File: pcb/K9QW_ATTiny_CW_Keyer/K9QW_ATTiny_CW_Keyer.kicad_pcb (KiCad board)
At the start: 2 copper layers, 50.8 x 31.8 mm, 33 parts, among them J1 Power Input, J2 AudioJack4, J3 AudioJack4, J4 Sidetone, J5 Mounting Hole, Q1 AO3401A, Q2 MMBT3904, Q3 MMBT2222A, Q4 MMBT3904, SW1 Power Switch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

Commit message: Routing signals
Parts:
- moved R4 25.6 mm to (151.8, 90.4), turned to 0 degrees
- moved Q2 24.4 mm to (155.8, 91.3)
- moved C6 16.0 mm to (161.4, 107.1), turned to 180 degrees
- moved Q3 9.10 mm to (146.3, 91.4), turned to -90 degrees
- moved D2 1.00 mm to (173.6, 97.6), turned to 180 degrees
- moved R5 0.66 mm to (169.3, 97.6)
- moved R3 0.10 mm to (155.3, 105.4)
- moved Q1 0.06 mm to (136.6, 106.1)
- turned R6 to 180 degrees
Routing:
- net Net-(Q3-C): track 0.21 -> 56.2 mm
- net VCC: track 0.15 -> 52.1 mm
- net COMMAND: track 0.00 -> 29.3 mm
- net Net-(D2-K): track 0.00 -> 25.6 mm
- net Net-(D1-K): track 0.00 -> 22.8 mm
- net SIDETONE: track 0.00 -> 21.2 mm
- net VDC: track 0.00 -> 15.4 mm
- net Net-(D3-K): track 0.00 -> 14.9 mm
- net Net-(JP1-A): track 0.00 -> 14.7 mm
- net DAH: track 0.00 -> 14.5 mm
- net DIT: track 0.00 -> 9.48 mm
- net KEY: track 0.00 -> 5.96 mm
- net Net-(D1-A): track 0.00 -> 5.27 mm
- net Net-(SW1-A): track 0.00 -> 5.18 mm
- net Net-(Q3-B): track 0.02 -> 4.41 mm
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
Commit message: Refining layout
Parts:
- moved Q4 10.9 mm to (151.0, 113.7), turned to -90 degrees
- moved SW2 7.91 mm to (167.7, 111.2), turned to 0 degrees
- moved R8 6.43 mm to (155.3, 107.1), turned to 180 degrees
- moved R7 5.73 mm to (153.9, 113.6), turned to 90 degrees
- moved D3 4.91 mm to (153.9, 109.9)
- moved J4 4.45 mm to (158.5, 111.3), turned to 0 degrees
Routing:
- net Net-(D3-K): track 14.9 -> 5.82 mm
- net SIDETONE: track 21.2 -> 25.0 mm
- net COMMAND: track 29.3 -> 27.4 mm
- net VCC: track 52.1 -> 53.9 mm
- net Net-(D3-A): track 1.90 -> 3.12 mm
- net GND: track 0.00 -> 0.83 mm, vias 8 -> 6
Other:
- board text added: "S"

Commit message: Minor adjustments
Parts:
- moved C1 4.72 mm to (148.4, 102.7), turned to 180 degrees
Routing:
- net VCC: track 53.9 -> 54.5 mm
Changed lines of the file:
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@@
 	(footprint "Capacitor_SMD:C_0603_1608Metric_Pad1.08x0.95mm_HandSolder"
 		(layer "F.Cu")
-		(at 151.5364 106.2239 -90)
+		(at 148.4122 102.6922 180)
 		(descr "Capacitor SMD 0603 (1608 Metric), square (rectangular) end terminal, IPC_7351 nominal with elongated pad for handsoldering. (Body size source: IPC-SM-782 page 76, https://www.pcb-3d.com/wordpress/wp-content/uploads/ipc-sm-782a_amendment_1_and_2.pdf), generated with kicad-footprint-generator")
 		(tags "capacitor handsolder")
 		(property "Reference" "C1"
-			(at -0.0011 -1.4732 90)
+			(at -0.0011 -1.4732 360)
 			(layer "F.SilkS")
 			(effects
@@
 		)
 		(property "Value" "100nF"
-			(at 0 1.43 90)
+			(at 0 1.43 360)
 			(layer "F.Fab")
 			(effects
@@
 		)
 		(property "Footprint" "Capacitor_SMD:C_0603_1608Metric_Pad1.08x0.95mm_HandSolder"
-			(at 0 0 -90)
+			(at 0 0 180)
 			(unlocked yes)
 			(layer "F.Fab")
@@
 		)
 		(property "Datasheet" ""
-			(at 0 0 -90)
+			(at 0 0 180)
 			(unlocked yes)
 			(layer "F.Fab")
@@
 		)
 		(property "Description" "Unpolarized capacitor"
-			(at 0 0 -90)
+			(at 0 0 180)
 			(unlocked yes)
 			(layer "F.Fab")
@@
 		)
 		(fp_line
-			(start -1.65 0.73)
-			(end -1.65 -0.73)
+			(start 1.65 0.73)
+			(end -1.65 0.73)
 			(stroke
 				(width 0.05)
@@
 		)
 		(fp_line
-			(start 1.65 0.73)
-			(end -1.65 0.73)
+			(start 1.65 -0.73)
+			(end 1.65 0.73)
 			(stroke
 				(width 0.05)
@@
 		)
 		(fp_line
-			(start -1.65 -0.73)
-			(end 1.65 -0.73)
+			(start -1.65 0.73)
+			(end -1.65 -0.73)
 			(stroke
 				(width 0.05)
@@
 		)
 		(fp_line
-			(start 1.65 -0.73)
-			(end 1.65 0.73)
+			(start -1.65 -0.73)
+			(end 1.65 -0.73)
 			(stroke
 				(width 0.05)
@@
 		)
 		(fp_line
-			(start -0.8 0.4)
-			(end -0.8 -0.4)
+			(start 0.8 0.4)
+			(end -0.8 0.4)
 			(stroke
 				(width 0.1)
@@
 		)
 		(fp_line
-			(start 0.8 0.4)
-			(end -0.8 0.4)
+			(start 0.8 -0.4)
+			(end 0.8 0.4)
 			(stroke
 				(width 0.1)
@@
 		)
 		(fp_line
-			(start -0.8 -0.4)
-			(end 0.8 -0.4)
+			(start -0.8 0.4)
+			(end -0.8 -0.4)
 			(stroke
 				(width 0.1)
@@
 		)
 		(fp_line
-			(start 0.8 -0.4)
-			(end 0.8 0.4)
+			(start -0.8 -0.4)
+			(end 0.8 -0.4)
 			(stroke
 				(width 0.1)
@@
 		)
 		(fp_text user "${REFERENCE}"
-			(at 0 0 90)
+			(at 0 0 360)
 			(layer "F.Fab")
 			(effects
@@
 		)
 		(pad "1" smd roundrect
-			(at -0.8625 0 270)
+			(at -0.8625 0 180)
 			(size 1.075 0.95)
 			(layers "F.Cu" "F.Paste" "F.Mask")
@@
 		)
 		(pad "2" smd roundrect
-			(at 0.8625 0 270)
+			(at 0.8625 0 180)
 			(size 1.075 0.95)
 			(layers "F.Cu" "F.Paste" "F.Mask")
@@
 	)
 	(segment
+		(start 151.7612 102.6884)
+		(end 151.401 102.6884)
+		(width 0.2)
+		(layer "F.Cu")
+		(net 1)
+	)
+	(segment
+		(start 149.2785 102.6884)
+		(end 149.2747 102.6922)
+		(width 1)
+		(layer "F.Cu")
+		(net 1)
+	)
+	(segment
+		(start 154.4358 105.3592)
+		(end 154.432 105.3592)
+		(width 0.2)
+		(layer "F.Cu")
+		(net 1)
+	)
+	(segment
 		(start 139.461 110.744)
 		(end 137.175 113.03)
@@
 	)
 	(segment
-		(start 151.5364 102.8238)
-		(end 151.401 102.6884)
-		(width 1)
+		(start 154.432 105.3592)
+		(end 151.7612 102.6884)
+		(width 0.2)
 		(layer "F.Cu")
 		(net 1)
 	)
 	(segment
-		(start 151.5364 105.3614)
-		(end 154.4336 105.3614)
-		(width 0.2)
+		(start 151.5364 102.8238)
+		(end 151.401 102.6884)
+		(width 1)
 		(layer "F.Cu")
 		(net 1)
@@
 	)
 	(segment
-		(start 151.6434 105.2544)
-		(end 151.5364 105.3614)
-		(width 0.2)
-		(layer "F.Cu")
-		(net 1)
-	)
-	(segment
 		(start 164.7314 106.1342)
 		(end 168.4058 102.4598)
@@
 	)
 	(segment
-		(start 151.5364 105.3614)
-		(end 151.5364 102.8238)
+		(start 146.5315 110.7455)
+		(end 146.533 110.744)
 		(width 1)
 		(layer "F.Cu")
@@
 	)
 	(segment
-		(start 146.5315 110.7455)
-		(end 146.533 110.744)
+		(start 151.401 102.6884)
+		(end 149.2785 102.6884)
 		(width 1)
 		(layer "F.Cu")

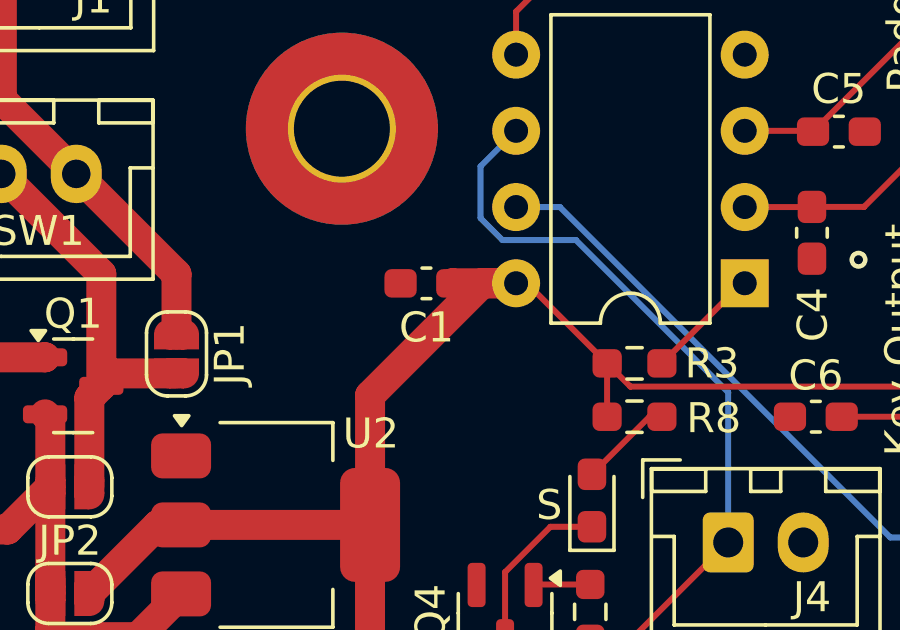
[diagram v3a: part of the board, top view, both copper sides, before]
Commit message: Filter cap for command button
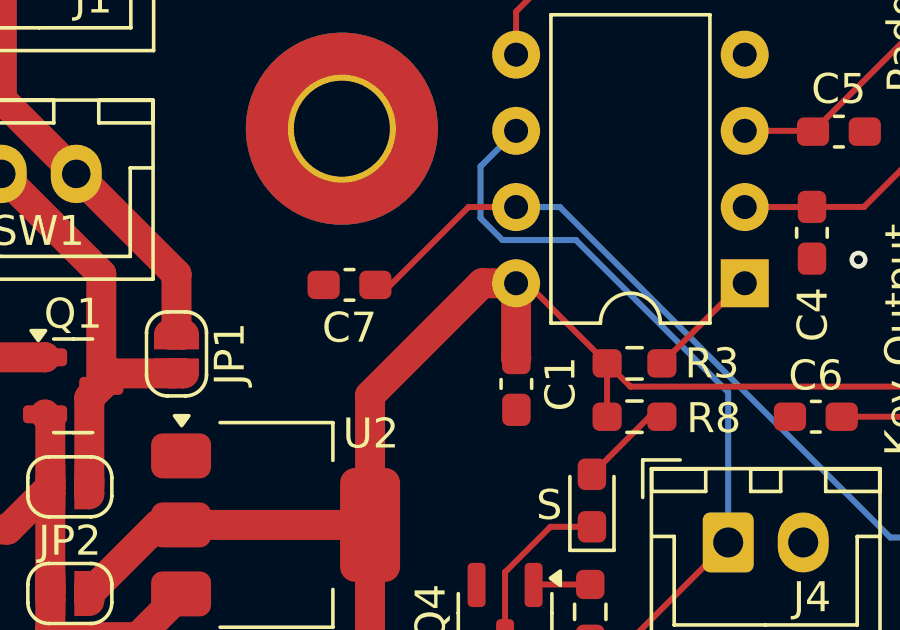
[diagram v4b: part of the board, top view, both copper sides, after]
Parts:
- added C7: 10nF, Capacitor_SMD:C_0603_1608Metric_Pad1.08x0.95mm_HandSolder, F.Cu at (145.8, 102.7)
- moved C1 4.50 mm to (151.4, 106.0), turned to -90 degrees
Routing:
- net COMMAND: track 27.4 -> 33.2 mm
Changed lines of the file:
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@@
 		)
 	)
+	(footprint "Capacitor_SMD:C_0603_1608Metric_Pad1.08x0.95mm_HandSolder"
+		(layer "F.Cu")
+		(at 145.8468 102.743 180)
+		(descr "Capacitor SMD 0603 (1608 Metric), square (rectangular) end terminal, IPC_7351 nominal with elongated pad for handsoldering. (Body size source: IPC-SM-782 page 76, https://www.pcb-3d.com/wordpress/wp-content/uploads/ipc-sm-782a_amendment_1_and_2.pdf), generated with kicad-footprint-generator")
+		(tags "capacitor handsolder")
+		(property "Reference" "C7"
+			(at 0 -1.43 360)
+			(layer "F.SilkS")
+			(effects
+				(font
+					(size 1 1)
+					(thickness 0.15)
+				)
+			)
+		)
+		(property "Value" "10nF"
+			(at 0 1.43 360)
+			(layer "F.Fab")
+			(effects
+				(font
+					(size 1 1)
+					(thickness 0.15)
+				)
+			)
+		)
+		(property "Footprint" "Capacitor_SMD:C_0603_1608Metric_Pad1.08x0.95mm_HandSolder"
+			(at 0 0 180)
+			(unlocked yes)
+			(layer "F.Fab")
+			(hide yes)
+			(effects
+				(font
+					(size 1.27 1.27)
+					(thickness 0.15)
+				)
+			)
+		)
+		(property "Datasheet" ""
+			(at 0 0 180)
+			(unlocked yes)
+			(layer "F.Fab")
+			(hide yes)
+			(effects
+				(font
+					(size 1.27 1.27)
+					(thickness 0.15)
+				)
+			)
+		)
+		(property "Description" "Unpolarized capacitor"
+			(at 0 0 180)
+			(unlocked yes)
+			(layer "F.Fab")
+			(hide yes)
+			(effects
+				(font
+					(size 1.27 1.27)
+					(thickness 0.15)
+				)
+			)
+		)
+		(property ki_fp_filters "C_*")
+		(sheetname "Root")
+		(sheetfile "K9QW_ATTiny_CW_Keyer.kicad_sch")
+		(attr smd)
+		(fp_line
+			(start -0.146267 0.51)
+			(end 0.146267 0.51)
+			(stroke
+				(width 0.12)
+				(type solid)
+			)
+			(layer "F.SilkS")
+		)
+		(fp_line
+			(start -0.146267 -0.51)
+			(end 0.146267 -0.51)
+			(stroke
+				(width 0.12)
+				(type solid)
+			)
+			(layer "F.SilkS")
+		)
+		(fp_line
+			(start 1.65 0.73)
+			(end -1.65 0.73)
+			(stroke
+				(width 0.05)
+				(type solid)
+			)
+			(layer "F.CrtYd")
+		)
+		(fp_line
+			(start 1.65 -0.73)
+			(end 1.65 0.73)
+			(stroke
+				(width 0.05)
+				(type solid)
+			)
+			(layer "F.CrtYd")
+		)
+		(fp_line
+			(start -1.65 0.73)
+			(end -1.65 -0.73)
+			(stroke
+				(width 0.05)
+				(type solid)
+			)
+			(layer "F.CrtYd")
+		)
+		(fp_line
+			(start -1.65 -0.73)
+			(end 1.65 -0.73)
+			(stroke
+				(width 0.05)
+				(type solid)
+			)
+			(layer "F.CrtYd")
+		)
+		(fp_line
+			(start 0.8 0.4)
+			(end -0.8 0.4)
+			(stroke
+				(width 0.1)
+				(type solid)
+			)
+			(layer "F.Fab")
+		)
+		(fp_line
+			(start 0.8 -0.4)
+			(end 0.8 0.4)
+			(stroke
+				(width 0.1)
+				(type solid)
+			)
+			(layer "F.Fab")
+		)
+		(fp_line
+			(start -0.8 0.4)
+			(end -0.8 -0.4)
+			(stroke
+				(width 0.1)
+				(type solid)
+			)
+			(layer "F.Fab")
+		)
+		(fp_line
+			(start -0.8 -0.4)
+			(end 0.8 -0.4)
+			(stroke
+				(width 0.1)
+				(type solid)
+			)
+			(layer "F.Fab")
+		)
+		(fp_text user "${REFERENCE}"
+			(at 0 0 360)
+			(layer "F.Fab")
+			(effects
+				(font
+					(size 0.4 0.4)
+					(thickness 0.06)
+				)
+			)
+		)
+		(pad "1" smd roundrect
+			(at -0.8625 0 180)
+			(size 1.075 0.95)
+			(layers "F.Cu" "F.Paste" "F.Mask")
+			(roundrect_rratio 0.25)
+			(net 7 "COMMAND")
+			(pintype "passive")
+		)
+		(pad "2" smd roundrect
+			(at 0.8625 0 180)
+			(size 1.075 0.95)
+			(layers "F.Cu" "F.Paste" "F.Mask")
+			(roundrect_rratio 0.25)
+			(net 2 "GND")
+			(pintype "passive")
+		)
+		(model "${KICAD8_3DMODEL_DIR}/Capacitor_SMD.3dshapes/C_0603_1608Metric.wrl"
+			(offset
+				(xyz 0 0 0)
+			)
+			(scale
+				(xyz 1 1 1)
+			)
+			(rotate
+				(xyz 0 0 0)
+			)
+		)
+	)
 	(footprint "Connector_Audio:Jack_3.5mm_PJ320D_Horizontal"
 		(layer "F.Cu")
@@
 	(footprint "Capacitor_SMD:C_0603_1608Metric_Pad1.08x0.95mm_HandSolder"
 		(layer "F.Cu")
-		(at 148.4122 102.6922 180)
+		(at 151.4094 106.045 -90)
 		(descr "Capacitor SMD 0603 (1608 Metric), square (rectangular) end terminal, IPC_7351 nominal with elongated pad for handsoldering. (Body size source: IPC-SM-782 page 76, https://www.pcb-3d.com/wordpress/wp-content/uploads/ipc-sm-782a_amendment_1_and_2.pdf), generated with kicad-footprint-generator")
 		(tags "capacitor handsolder")
 		(property "Reference" "C1"
-			(at -0.0011 -1.4732 360)
+			(at -0.0011 -1.4732 90)
 			(layer "F.SilkS")
 			(effects
@@
 		)
 		(property "Value" "100nF"
-			(at 0 1.43 360)
+			(at 0 1.43 90)
 			(layer "F.Fab")
 			(effects
@@
 		)
 		(property "Footprint" "Capacitor_SMD:C_0603_1608Metric_Pad1.08x0.95mm_HandSolder"
-			(at 0 0 180)
+			(at 0 0 -90)
 			(unlocked yes)
 			(layer "F.Fab")
@@
 		)
 		(property "Datasheet" ""
-			(at 0 0 180)
+			(at 0 0 -90)
 			(unlocked yes)
 			(layer "F.Fab")
@@
 		)
 		(property "Description" "Unpolarized capacitor"
-			(at 0 0 180)
+			(at 0 0 -90)
 			(unlocked yes)
 			(layer "F.Fab")
@@
 		)
 		(fp_line
-			(start 1.65 0.73)
-			(end -1.65 0.73)
+			(start -1.65 0.73)
+			(end -1.65 -0.73)
 			(stroke
 				(width 0.05)
@@
 		)
 		(fp_line
-			(start 1.65 -0.73)
-			(end 1.65 0.73)
+			(start 1.65 0.73)
+			(end -1.65 0.73)
 			(stroke
 				(width 0.05)
@@
 		)
 		(fp_line
-			(start -1.65 0.73)
-			(end -1.65 -0.73)
+			(start -1.65 -0.73)
+			(end 1.65 -0.73)
 			(stroke
 				(width 0.05)
@@
 		)
 		(fp_line
-			(start -1.65 -0.73)
-			(end 1.65 -0.73)
+			(start 1.65 -0.73)
+			(end 1.65 0.73)
 			(stroke
 				(width 0.05)
@@
 		)
 		(fp_line
-			(start 0.8 0.4)
-			(end -0.8 0.4)
+			(start -0.8 0.4)
+			(end -0.8 -0.4)
 			(stroke
 				(width 0.1)
@@
 		)
 		(fp_line
-			(start 0.8 -0.4)
-			(end 0.8 0.4)
+			(start 0.8 0.4)
+			(end -0.8 0.4)
 			(stroke
 				(width 0.1)
@@
 		)
 		(fp_line
-			(start -0.8 0.4)
-			(end -0.8 -0.4)
+			(start -0.8 -0.4)
+			(end 0.8 -0.4)
 			(stroke
 				(width 0.1)
@@
 		)
 		(fp_line
-			(start -0.8 -0.4)
-			(end 0.8 -0.4)
+			(start 0.8 -0.4)
+			(end 0.8 0.4)
 			(stroke
 				(width 0.1)
@@
 		)
 		(fp_text user "${REFERENCE}"
-			(at 0 0 360)
+			(at 0 0 90)
 			(layer "F.Fab")
 			(effects
@@
 		)
 		(pad "1" smd roundrect
-			(at -0.8625 0 180)
+			(at -0.8625 0 270)
 			(size 1.075 0.95)
 			(layers "F.Cu" "F.Paste" "F.Mask")
@@
 		)
 		(pad "2" smd roundrect
-			(at 0.8625 0 180)
+			(at 0.8625 0 270)
 			(size 1.075 0.95)
 			(layers "F.Cu" "F.Paste" "F.Mask")
@@
 	)
 	(segment
-		(start 149.2785 102.6884)
-		(end 149.2747 102.6922)
-		(width 1)
-		(layer "F.Cu")
-		(net 1)
-	)
-	(segment
 		(start 154.4358 105.3592)
 		(end 154.432 105.3592)
@@
 	)
 	(segment
+		(start 151.401 102.6884)
+		(end 151.401 105.1741)
+		(width 1)
+		(layer "F.Cu")
+		(net 1)
+	)
+	(segment
 		(start 150.26963 102.6884)
 		(end 151.401 102.6884)
@@
 	)
 	(segment
-		(start 151.401 102.6884)
-		(end 149.2785 102.6884)
+		(start 151.401 105.1741)
+		(end 151.4094 105.1825)
 		(width 1)
 		(layer "F.Cu")
@@
 	)
 	(segment
+		(start 147.2184 102.743)
+		(end 149.813 100.1484)
+		(width 0.2)
+		(layer "F.Cu")
+		(net 7)
+	)
+	(segment
+		(start 146.7093 102.743)
+		(end 147.2184 102.743)
+		(width 0.2)
+		(layer "F.Cu")
+		(net 7)
+	)
+	(segment
 		(start 167.7428 111.161)
 		(end 174.2428 111.161)
 		(width 0.2)
 		(layer "F.Cu")
+		(net 7)
+	)
+	(segment
+		(start 149.813 100.1484)
+		(end 151.401 100.1484)
+		(width 0.2)
+		(layer "F.Cu")

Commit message: Minor
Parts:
- moved C7 0.27 mm to (145.6, 102.6)
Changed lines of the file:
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@@
 	(footprint "Capacitor_SMD:C_0603_1608Metric_Pad1.08x0.95mm_HandSolder"
 		(layer "F.Cu")
-		(at 145.8468 102.743 180)
+		(at 145.6436 102.5652 180)
 		(descr "Capacitor SMD 0603 (1608 Metric), square (rectangular) end terminal, IPC_7351 nominal with elongated pad for handsoldering. (Body size source: IPC-SM-782 page 76, https://www.pcb-3d.com/wordpress/wp-content/uploads/ipc-sm-782a_amendment_1_and_2.pdf), generated with kicad-footprint-generator")
 		(tags "capacitor handsolder")
@@
 	)
 	(segment
-		(start 147.2184 102.743)
-		(end 149.813 100.1484)
+		(start 151.401 100.1484)
+		(end 149.7368 100.1484)
 		(width 0.2)
 		(layer "F.Cu")
@@
 	)
 	(segment
-		(start 146.7093 102.743)
-		(end 147.2184 102.743)
+		(start 147.32 102.5652)
+		(end 146.7093 102.5652)
 		(width 0.2)
 		(layer "F.Cu")
@@
 	)
 	(segment
-		(start 167.7428 111.161)
-		(end 174.2428 111.161)
+		(start 149.7368 100.1484)
+		(end 147.32 102.5652)
 		(width 0.2)
 		(layer "F.Cu")
@@
 	)
 	(segment
-		(start 149.813 100.1484)
-		(end 151.401 100.1484)
+		(start 167.7428 111.161)
+		(end 174.2428 111.161)
 		(width 0.2)
 		(layer "F.Cu")

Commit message: Minor
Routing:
- net GND: vias 6 -> 8
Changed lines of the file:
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@@
+	)
+	(via
+		(at 154.5844 90.424)
+		(size 0.6)
+		(drill 0.3)
+		(layers "F.Cu" "B.Cu")
+		(free yes)
+		(net 2)
 	)
 	(via
@@
 		(size 0.6)
 		(drill 0.3)
+		(layers "F.Cu" "B.Cu")
+		(free yes)
+		(net 2)
+	)
+	(via
+		(at 149.4028 91.1352)
+		(size 0.6)
+		(drill 0.3)
